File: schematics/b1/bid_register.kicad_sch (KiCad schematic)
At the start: 13 parts, among them SW4 SW_DIP_x08, U3 74HC165

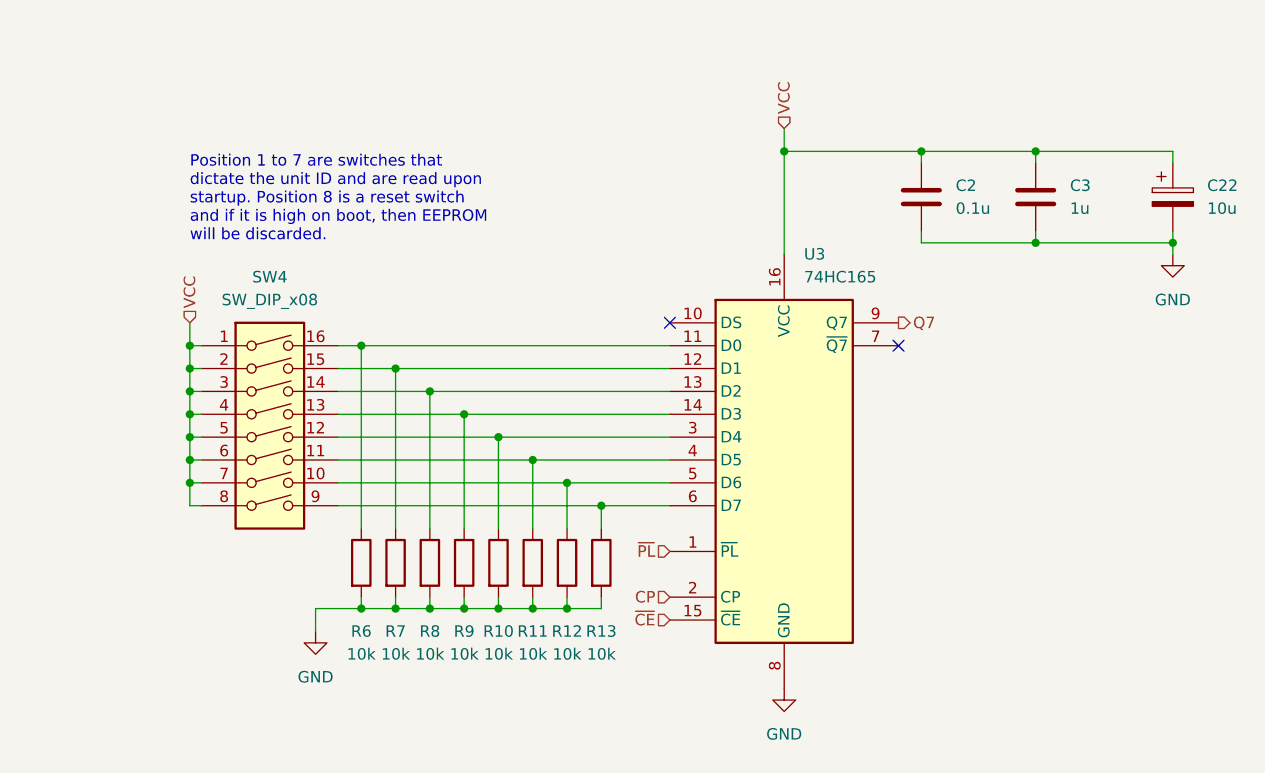
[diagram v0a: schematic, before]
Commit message: Updated the BID register.
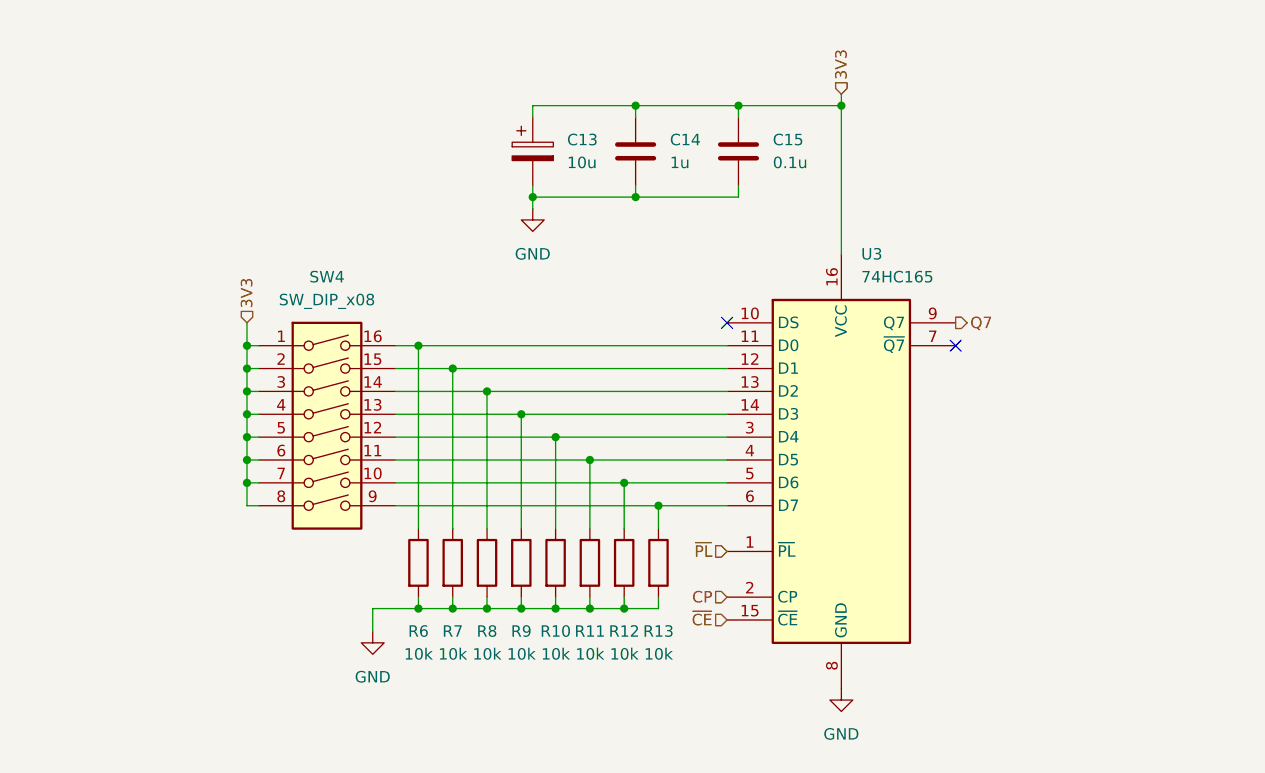
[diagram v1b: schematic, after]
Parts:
- removed C2: 0.1u, symbol Device:C
- removed C22: 10u, symbol Device:C_Polarized
- removed C3: 1u, symbol Device:C
- added C13: 10u, symbol Device:C_Polarized
- added C14: 1u, symbol Device:C
- added C15: 0.1u, symbol Device:C
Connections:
- net GND: now also C13.2, C14.2, C15.2
- net VCC renamed 3V3
- net 3V3: now also C13.1, C14.1, C15.1
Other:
- note removed: "Position 1 to 7 are switches that dictate the unit ID and are read upon startup. Position 8 is a reset switch and if it is high on boot, then EEPROM will be discarded."
- title: Initial State Register -> BID Register
- moved on the sheet: R10, R11, R12, R13, R6, R7, R8, R9, SW4, U3

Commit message: Added a bunch of test points.
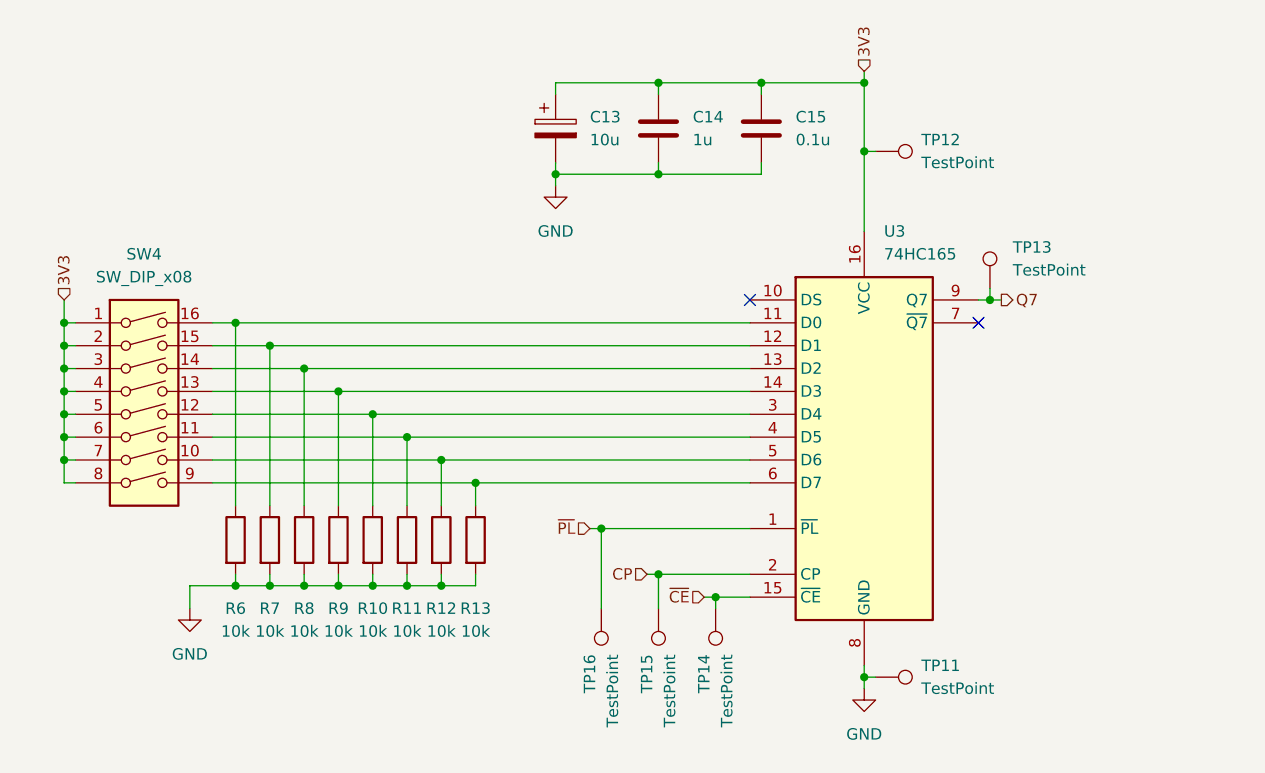
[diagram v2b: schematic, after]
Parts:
- added TP11, TP12, TP13, TP14, TP15, TP16: TestPoint, symbol Connector:TestPoint
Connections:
- net 3V3: now also TP12.1
- net CP: now also TP15.1
- net GND: now also TP11.1
- net Q7: now also TP13.1
- net ~{CE}: now also TP14.1
- net ~{PL}: now also TP16.1
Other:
- moved on the sheet: C13, C14, C15, R10, R11, R12, R13, R6, R7, R8, R9, SW4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

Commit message: Updated annotations.
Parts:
- renumbered C13 to C18, C14 to C19, C15 to C20, SW4 to SW5, TP12 to TP26, TP13 to TP27, TP16 to TP28, TP15 to TP29, TP14 to TP30, TP11 to TP31, U3 to U5
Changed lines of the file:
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@@
   (symbol (lib_id "Connector:TestPoint") (at 96.52 82.55 180) (unit 1)
     (in_bom yes) (on_board yes) (dnp no)
-    (property "Reference" "TP16" (at 95.25 87.63 90)
+    (property "Reference" "TP28" (at 96.52 87.63 90)
       (effects (font (size 1.27 1.27)) (justify left))
     )
     (property "Value" "TestPoint" (at 97.79 87.63 90)
-      (effects (font (size 1.27 1.27)) (justify left))
+      (effects (font (size 1.27 1.27)) (justify left) hide)
     )
     (property "Footprint" "" (at 91.44 82.55 0)
@@
       (project "b1"
         (path "/d6142fa5-2354-4512-9919-37616259c364/15951702-f191-4c4b-b68c-efdb5de618b5"
-          (reference "TP16") (unit 1)
+          (reference "TP28") (unit 1)
         )
       )
@@
   (symbol (lib_id "Switch:SW_DIP_x08") (at 45.72 60.96 0) (unit 1)
     (in_bom yes) (on_board yes) (dnp no) (fields_autoplaced)
-    (property "Reference" "SW4" (at 45.72 43.18 0)
+    (property "Reference" "SW5" (at 45.72 43.18 0)
       (effects (font (size 1.27 1.27)))
     )
@@
       (project "b1"
         (path "/d6142fa5-2354-4512-9919-37616259c364/15951702-f191-4c4b-b68c-efdb5de618b5"
-          (reference "SW4") (unit 1)
+          (reference "SW5") (unit 1)
         )
       )
@@
   (symbol (lib_id "Device:C") (at 102.87 29.21 0) (unit 1)
     (in_bom yes) (on_board yes) (dnp no) (fields_autoplaced)
-    (property "Reference" "C14" (at 106.68 27.94 0)
+    (property "Reference" "C19" (at 106.68 27.94 0)
       (effects (font (size 1.27 1.27)) (justify left))
     )
@@
       (project "b1"
         (path "/d6142fa5-2354-4512-9919-37616259c364/15951702-f191-4c4b-b68c-efdb5de618b5"
-          (reference "C14") (unit 1)
+          (reference "C19") (unit 1)
         )
       )
@@
   (symbol (lib_id "Connector:TestPoint") (at 102.87 82.55 180) (unit 1)
     (in_bom yes) (on_board yes) (dnp no)
-    (property "Reference" "TP15" (at 101.6 87.63 90)
+    (property "Reference" "TP29" (at 102.87 87.63 90)
       (effects (font (size 1.27 1.27)) (justify left))
     )
     (property "Value" "TestPoint" (at 104.14 87.63 90)
-      (effects (font (size 1.27 1.27)) (justify left))
+      (effects (font (size 1.27 1.27)) (justify left) hide)
     )
     (property "Footprint" "" (at 97.79 82.55 0)
@@
       (project "b1"
         (path "/d6142fa5-2354-4512-9919-37616259c364/15951702-f191-4c4b-b68c-efdb5de618b5"
-          (reference "TP15") (unit 1)
+          (reference "TP29") (unit 1)
         )
       )
@@
   (symbol (lib_id "Connector:TestPoint") (at 109.22 82.55 180) (unit 1)
     (in_bom yes) (on_board yes) (dnp no)
-    (property "Reference" "TP14" (at 107.95 87.63 90)
+    (property "Reference" "TP30" (at 109.22 87.63 90)
       (effects (font (size 1.27 1.27)) (justify left))
     )
     (property "Value" "TestPoint" (at 110.49 87.63 90)
-      (effects (font (size 1.27 1.27)) (justify left))
+      (effects (font (size 1.27 1.27)) (justify left) hide)
     )
     (property "Footprint" "" (at 104.14 82.55 0)
@@
       (project "b1"
         (path "/d6142fa5-2354-4512-9919-37616259c364/15951702-f191-4c4b-b68c-efdb5de618b5"
-          (reference "TP14") (unit 1)
+          (reference "TP30") (unit 1)
         )
       )
@@
   )
   (symbol (lib_id "Connector:TestPoint") (at 127 90.17 270) (unit 1)
-    (in_bom yes) (on_board yes) (dnp no) (fields_autoplaced)
-    (property "Reference" "TP11" (at 132.08 88.9 90)
+    (in_bom yes) (on_board yes) (dnp no)
+    (property "Reference" "TP31" (at 132.08 90.17 90)
       (effects (font (size 1.27 1.27)) (justify left))
     )
     (property "Value" "TestPoint" (at 132.08 91.44 90)
-      (effects (font (size 1.27 1.27)) (justify left))
+      (effects (font (size 1.27 1.27)) (justify left) hide)
     )
     (property "Footprint" "" (at 127 95.25 0)
@@
       (project "b1"
         (path "/d6142fa5-2354-4512-9919-37616259c364/15951702-f191-4c4b-b68c-efdb5de618b5"
-          (reference "TP11") (unit 1)
+          (reference "TP31") (unit 1)
         )
       )
@@
   )
   (symbol (lib_id "Connector:TestPoint") (at 127 31.75 270) (unit 1)
-    (in_bom yes) (on_board yes) (dnp no) (fields_autoplaced)
-    (property "Reference" "TP12" (at 132.08 30.48 90)
+    (in_bom yes) (on_board yes) (dnp no)
+    (property "Reference" "TP26" (at 132.08 31.75 90)
       (effects (font (size 1.27 1.27)) (justify left))
     )
     (property "Value" "TestPoint" (at 132.08 33.02 90)
-      (effects (font (size 1.27 1.27)) (justify left))
+      (effects (font (size 1.27 1.27)) (justify left) hide)
     )
     (property "Footprint" "" (at 127 36.83 0)
@@
       (project "b1"
         (path "/d6142fa5-2354-4512-9919-37616259c364/15951702-f191-4c4b-b68c-efdb5de618b5"
-          (reference "TP12") (unit 1)
+          (reference "TP26") (unit 1)
         )
       )
@@
   (symbol (lib_id "power:GND") (at 50.8 82.55 0) (unit 1)
     (in_bom yes) (on_board yes) (dnp no) (fields_autoplaced)
-    (property "Reference" "#PWR07" (at 50.8 88.9 0)
+    (property "Reference" "#PWR027" (at 50.8 88.9 0)
       (effects (font (size 1.27 1.27)) hide)
     )
@@
       (project "b1"
         (path "/d6142fa5-2354-4512-9919-37616259c364/15951702-f191-4c4b-b68c-efdb5de618b5"
-          (reference "#PWR07") (unit 1)
+          (reference "#PWR027") (unit 1)
         )
       )
@@
   (symbol (lib_id "Device:C") (at 114.3 29.21 0) (unit 1)
     (in_bom yes) (on_board yes) (dnp no)
-    (property "Reference" "C15" (at 118.11 27.94 0)
+    (property "Reference" "C20" (at 118.11 27.94 0)
       (effects (font (size 1.27 1.27)) (justify left))
     )
@@
       (project "b1"
         (path "/d6142fa5-2354-4512-9919-37616259c364/15951702-f191-4c4b-b68c-efdb5de618b5"
-          (reference "C15") (unit 1)
+          (reference "C20") (unit 1)
         )
       )
@@
   (symbol (lib_id "Device:C_Polarized") (at 91.44 29.21 0) (unit 1)
     (in_bom yes) (on_board yes) (dnp no)
-    (property "Reference" "C13" (at 95.25 27.94 0)
+    (property "Reference" "C18" (at 95.25 27.94 0)
       (effects (font (size 1.27 1.27)) (justify left))
     )
@@
       (project "b1"
         (path "/d6142fa5-2354-4512-9919-37616259c364/15951702-f191-4c4b-b68c-efdb5de618b5"
-          (reference "C13") (unit 1)
+          (reference "C18") (unit 1)
         )
       )
@@
   (symbol (lib_id "74xx:74HC165") (at 125.73 63.5 0) (unit 1)
     (in_bom yes) (on_board yes) (dnp no) (fields_autoplaced)
-    (property "Reference" "U3" (at 127.9241 40.64 0)
+    (property "Reference" "U5" (at 127.9241 40.64 0)
       (effects (font (size 1.27 1.27)) (justify left))
     )
@@
       (project "b1"
         (path "/d6142fa5-2354-4512-9919-37616259c364/15951702-f191-4c4b-b68c-efdb5de618b5"
-          (reference "U3") (unit 1)
+          (reference "U5") (unit 1)
         )
       )
@@
   (symbol (lib_id "power:GND") (at 125.73 91.44 0) (unit 1)
     (in_bom yes) (on_board yes) (dnp no)
-    (property "Reference" "#PWR030" (at 125.73 97.79 0)
+    (property "Reference" "#PWR028" (at 125.73 97.79 0)
       (effects (font (size 1.27 1.27)) hide)
     )
@@
       (project "b1"
         (path "/d6142fa5-2354-4512-9919-37616259c364/15951702-f191-4c4b-b68c-efdb5de618b5"
-          (reference "#PWR030") (unit 1)
+          (reference "#PWR028") (unit 1)
         )
       )
@@
   (symbol (lib_id "power:GND") (at 91.44 35.56 0) (unit 1)
     (in_bom yes) (on_board yes) (dnp no) (fields_autoplaced)
-    (property "Reference" "#PWR022" (at 91.44 41.91 0)
+    (property "Reference" "#PWR026" (at 91.44 41.91 0)
       (effects (font (size 1.27 1.27)) hide)
     )
@@
       (project "b1"
         (path "/d6142fa5-2354-4512-9919-37616259c364/15951702-f191-4c4b-b68c-efdb5de618b5"
-          (reference "#PWR022") (unit 1)
+          (reference "#PWR026") (unit 1)
         )
       )
@@
   )
   (symbol (lib_id "Connector:TestPoint") (at 139.7 46.99 0) (unit 1)
-    (in_bom yes) (on_board yes) (dnp no) (fields_autoplaced)
-    (property "Reference" "TP13" (at 142.24 42.418 0)
-      (effects (font (size 1.27 1.27)) (justify left))
+    (in_bom yes) (on_board yes) (dnp no)
+    (property "Reference" "TP27" (at 139.7 40.64 0)
+      (effects (font (size 1.27 1.27)))
     )
     (property "Value" "TestPoint" (at 142.24 44.958 0)
-      (effects (font (size 1.27 1.27)) (justify left))
+      (effects (font (size 1.27 1.27)) (justify left) hide)
     )
     (property "Footprint" "" (at 144.78 46.99 0)
@@
       (project "b1"
         (path "/d6142fa5-2354-4512-9919-37616259c364/15951702-f191-4c4b-b68c-efdb5de618b5"
-          (reference "TP13") (unit 1)
-        )
-      )
+          (reference "TP27") (unit 1)
+        )
+      )

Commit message: Finalizing touches to the B1 schematic.
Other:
- moved on the sheet: R10, R11, R12, R13, R6, R7, R8, SW5

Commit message: Assigned some footprints.
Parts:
- C18: footprint (none) -> Capacitor_THT:CP_Radial_D4.0mm_P2.00mm
- C19, C20: footprint (none) -> Capacitor_SMD:C_1206_3216Metric_Pad1.33x1.80mm_HandSolder
- R10, R11, R12, R13, R6, R7, R8, R9: footprint (none) -> Resistor_SMD:R_1206_3216Metric_Pad1.30x1.75mm_HandSolder
- SW5: footprint (none) -> Button_Switch_THT:SW_DIP_SPSTx08_Slide_6.7x21.88mm_W7.62mm_P2.54mm_LowProfile
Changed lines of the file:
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@@
       (effects (font (size 1.27 1.27)))
     )
-    (property "Footprint" "" (at 80.772 74.93 90)
+    (property "Footprint" "Resistor_SMD:R_1206_3216Metric_Pad1.30x1.75mm_HandSolder" (at 80.772 74.93 90)
       (effects (font (size 1.27 1.27)) hide)
     )
@@
       (effects (font (size 1.27 1.27)))
     )
-    (property "Footprint" "" (at 41.91 60.96 0)
+    (property "Footprint" "Button_Switch_THT:SW_DIP_SPSTx08_Slide_6.7x21.88mm_W7.62mm_P2.54mm_LowProfile" (at 41.91 60.96 0)
       (effects (font (size 1.27 1.27)) hide)
     )
@@
       (effects (font (size 1.27 1.27)))
     )
-    (property "Footprint" "" (at 70.612 74.93 90)
+    (property "Footprint" "Resistor_SMD:R_1206_3216Metric_Pad1.30x1.75mm_HandSolder" (at 70.612 74.93 90)
       (effects (font (size 1.27 1.27)) hide)
     )
@@
       (effects (font (size 1.27 1.27)) (justify left))
     )
-    (property "Footprint" "" (at 103.8352 33.02 0)
+    (property "Footprint" "Capacitor_SMD:C_1206_3216Metric_Pad1.33x1.80mm_HandSolder" (at 103.8352 33.02 0)
       (effects (font (size 1.27 1.27)) hide)
     )
@@
       (effects (font (size 1.27 1.27)))
     )
-    (property "Footprint" "" (at 85.852 74.93 90)
+    (property "Footprint" "Resistor_SMD:R_1206_3216Metric_Pad1.30x1.75mm_HandSolder" (at 85.852 74.93 90)
       (effects (font (size 1.27 1.27)) hide)
     )
@@
       (effects (font (size 1.27 1.27)))
     )
-    (property "Footprint" "" (at 75.692 74.93 90)
+    (property "Footprint" "Resistor_SMD:R_1206_3216Metric_Pad1.30x1.75mm_HandSolder" (at 75.692 74.93 90)
       (effects (font (size 1.27 1.27)) hide)
     )
@@
       (effects (font (size 1.27 1.27)))
     )
-    (property "Footprint" "" (at 55.372 74.93 90)
+    (property "Footprint" "Resistor_SMD:R_1206_3216Metric_Pad1.30x1.75mm_HandSolder" (at 55.372 74.93 90)
       (effects (font (size 1.27 1.27)) hide)
     )
@@
       (effects (font (size 1.27 1.27)))
     )
-    (property "Footprint" "" (at 50.292 74.93 90)
+    (property "Footprint" "Resistor_SMD:R_1206_3216Metric_Pad1.30x1.75mm_HandSolder" (at 50.292 74.93 90)
       (effects (font (size 1.27 1.27)) hide)
     )
@@
       (effects (font (size 1.27 1.27)) (justify left))
     )
-    (property "Footprint" "" (at 115.2652 33.02 0)
+    (property "Footprint" "Capacitor_SMD:C_1206_3216Metric_Pad1.33x1.80mm_HandSolder" (at 115.2652 33.02 0)
       (effects (font (size 1.27 1.27)) hide)
     )
@@
       (effects (font (size 1.27 1.27)) (justify left))
     )
-    (property "Footprint" "" (at 92.4052 33.02 0)
+    (property "Footprint" "Capacitor_THT:CP_Radial_D4.0mm_P2.00mm" (at 92.4052 33.02 0)
       (effects (font (size 1.27 1.27)) hide)
     )
@@
       (effects (font (size 1.27 1.27)))
     )
-    (property "Footprint" "" (at 65.532 74.93 90)
+    (property "Footprint" "Resistor_SMD:R_1206_3216Metric_Pad1.30x1.75mm_HandSolder" (at 65.532 74.93 90)
       (effects (font (size 1.27 1.27)) hide)
     )
@@
       (effects (font (size 1.27 1.27)))
     )
-    (property "Footprint" "" (at 60.452 74.93 90)
-      (effects (font (size 1.27 1.27)) hide)
-    )
+    (property "Footprint" "Resistor_SMD:R_1206_3216Metric_Pad1.30x1.75mm_HandSolder" (at 60.452 74.93 90)
+      (effects (font (size 1.27 1.27)) hide)
+    )

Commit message: Finished assigning footprints.
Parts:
- TP26, TP27, TP28, TP29, TP30, TP31: footprint (none) -> TestPoint:TestPoint_Loop_D2.50mm_Drill1.0mm
- U5: footprint (none) -> SN74HC595N:DIP794W45P254L1969H508Q16
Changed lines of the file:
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@@
       (effects (font (size 1.27 1.27)) (justify left) hide)
     )
-    (property "Footprint" "" (at 91.44 82.55 0)
+    (property "Footprint" "TestPoint:TestPoint_Loop_D2.50mm_Drill1.0mm" (at 91.44 82.55 0)
       (effects (font (size 1.27 1.27)) hide)
     )
@@
       (effects (font (size 1.27 1.27)) (justify left) hide)
     )
-    (property "Footprint" "" (at 97.79 82.55 0)
+    (property "Footprint" "TestPoint:TestPoint_Loop_D2.50mm_Drill1.0mm" (at 97.79 82.55 0)
       (effects (font (size 1.27 1.27)) hide)
     )
@@
       (effects (font (size 1.27 1.27)) (justify left) hide)
     )
-    (property "Footprint" "" (at 104.14 82.55 0)
+    (property "Footprint" "TestPoint:TestPoint_Loop_D2.50mm_Drill1.0mm" (at 104.14 82.55 0)
       (effects (font (size 1.27 1.27)) hide)
     )
@@
       (effects (font (size 1.27 1.27)) (justify left) hide)
     )
-    (property "Footprint" "" (at 127 95.25 0)
+    (property "Footprint" "TestPoint:TestPoint_Loop_D2.50mm_Drill1.0mm" (at 127 95.25 0)
       (effects (font (size 1.27 1.27)) hide)
     )
@@
       (effects (font (size 1.27 1.27)) (justify left) hide)
     )
-    (property "Footprint" "" (at 127 36.83 0)
+    (property "Footprint" "TestPoint:TestPoint_Loop_D2.50mm_Drill1.0mm" (at 127 36.83 0)
       (effects (font (size 1.27 1.27)) hide)
     )
@@
       (effects (font (size 1.27 1.27)) (justify left))
     )
-    (property "Footprint" "" (at 125.73 63.5 0)
+    (property "Footprint" "SN74HC595N:DIP794W45P254L1969H508Q16" (at 125.73 63.5 0)
       (effects (font (size 1.27 1.27)) hide)
     )
@@
       (effects (font (size 1.27 1.27)) (justify left) hide)
     )
-    (property "Footprint" "" (at 144.78 46.99 0)
-      (effects (font (size 1.27 1.27)) hide)
-    )
+    (property "Footprint" "TestPoint:TestPoint_Loop_D2.50mm_Drill1.0mm" (at 144.78 46.99 0)
+      (effects (font (size 1.27 1.27)) hide)
+    )
